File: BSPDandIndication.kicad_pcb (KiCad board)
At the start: 2 copper layers, 51 parts, among them J1 SafetyIN, J2 Masa, J3 12VTelem, J4 Sensors, J5 LED, J6 BSPD12OUT, J7 SafetyReturn, K1 FINDER-36.11, Q1 BC817, U1 LM1117-5.0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

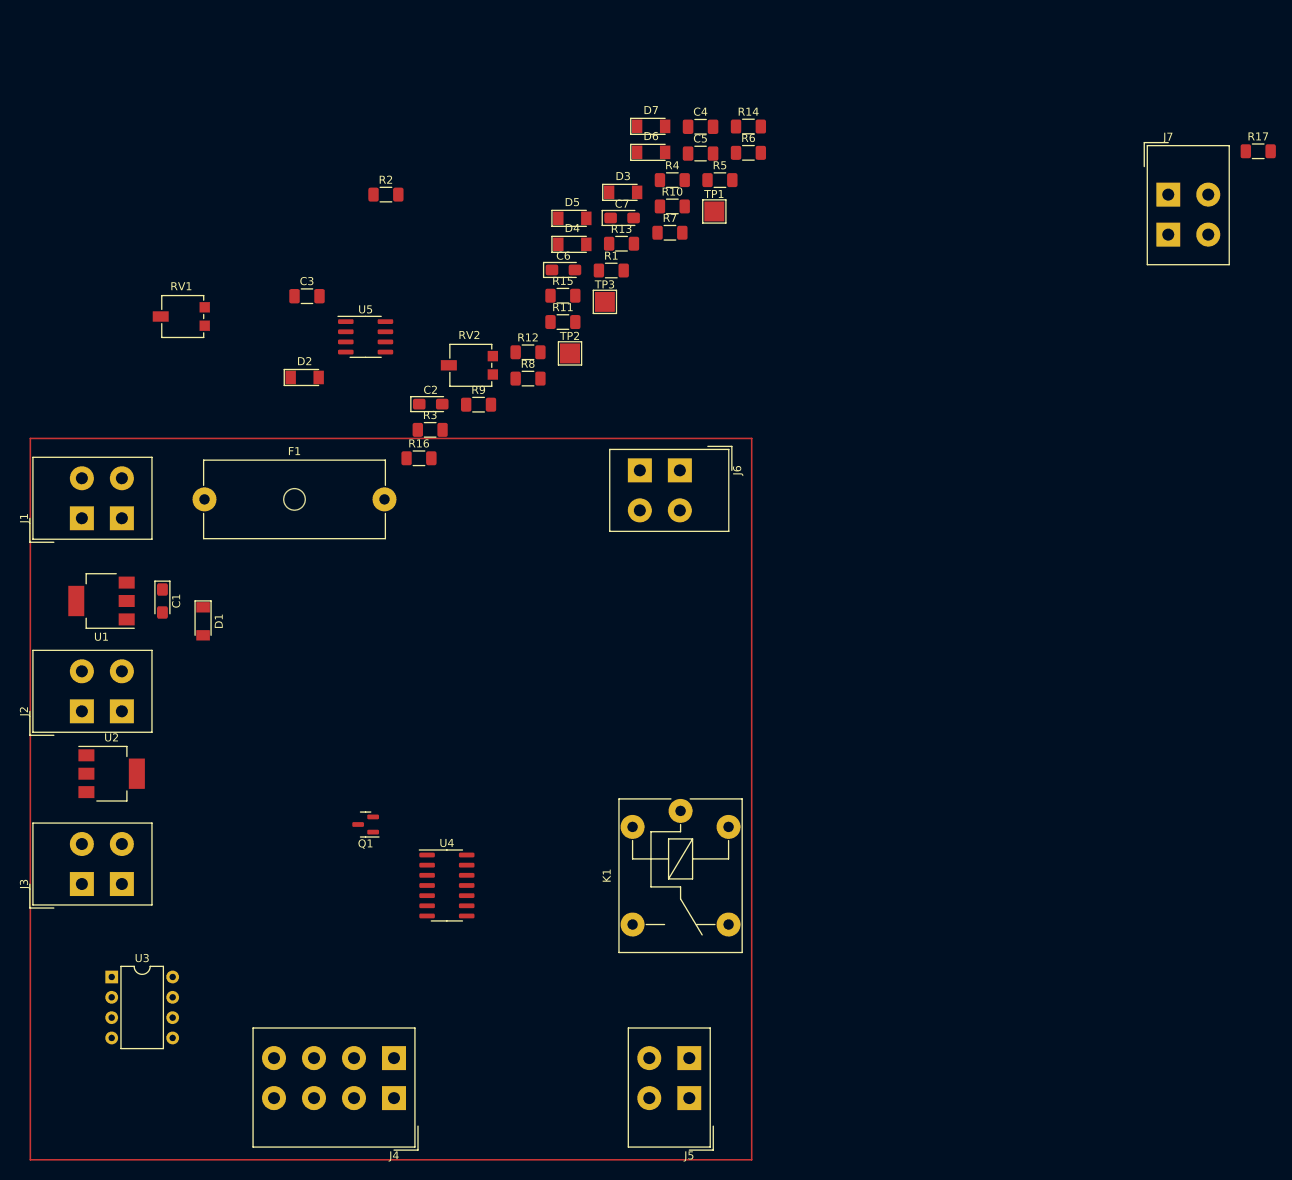
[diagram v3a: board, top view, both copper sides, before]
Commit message: Arrange components regarding PIC12f
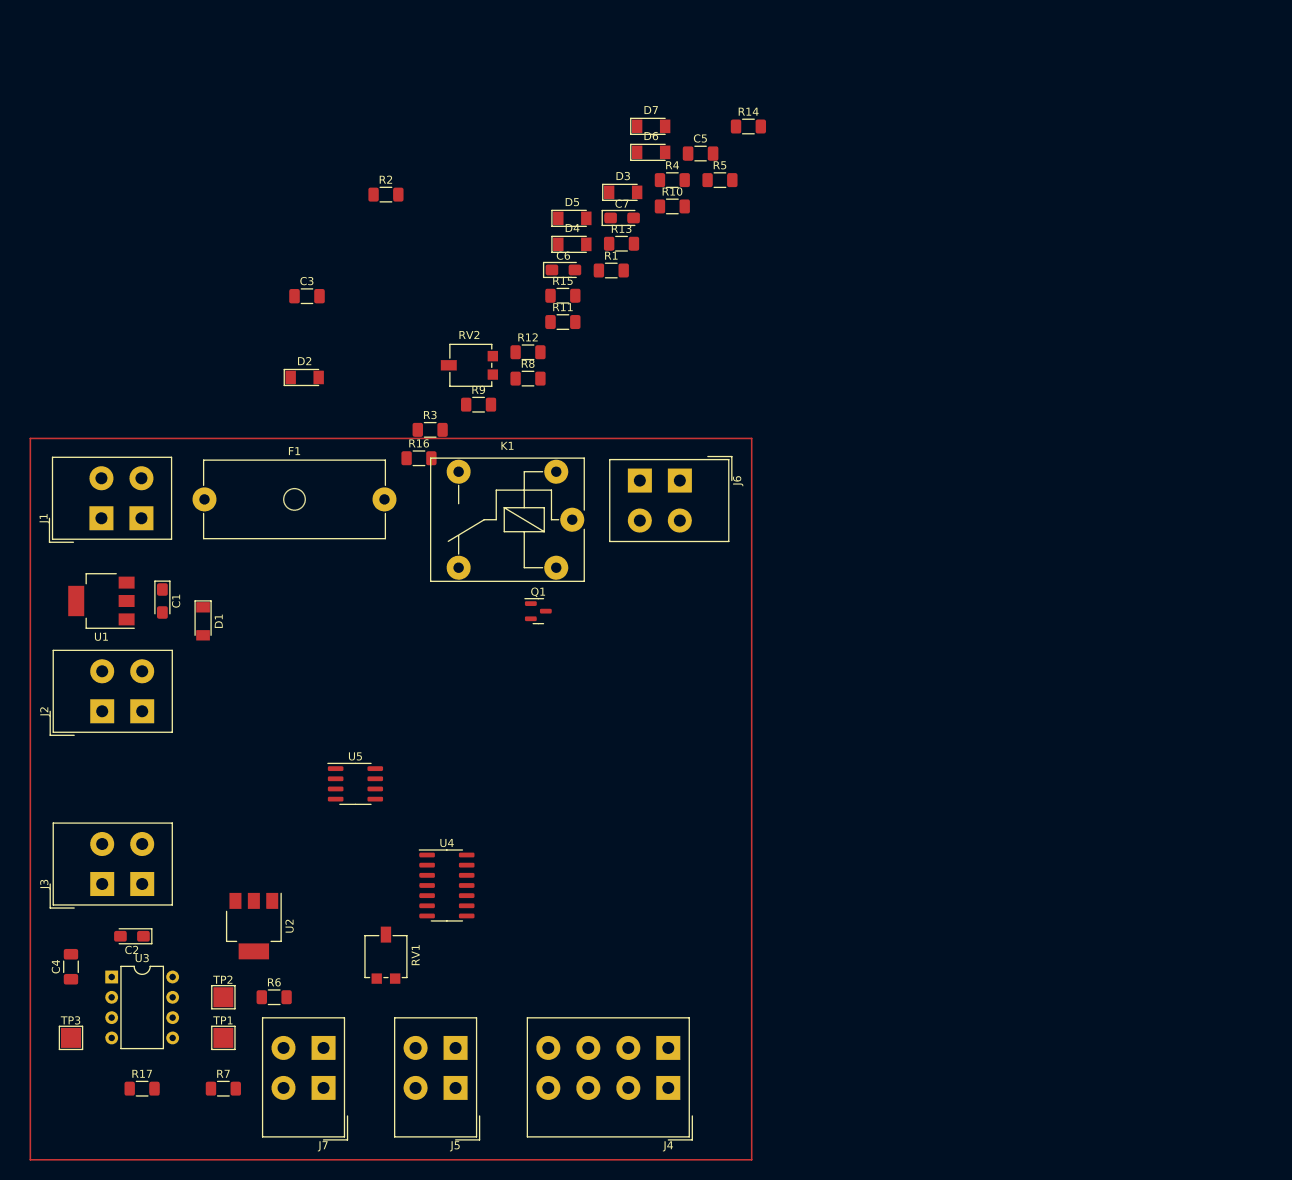
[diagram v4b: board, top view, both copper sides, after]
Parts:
- moved R17 182.2 mm to (30.5, 147.3)
- moved J7 153.7 mm to (53.2, 147.2), turned to 180 degrees
- moved C4 131.2 mm to (21.6, 132.1), turned to 90 degrees
- moved R6 121.1 mm to (47.0, 135.9)
- moved R7 120.7 mm to (40.6, 147.3)
- moved TP1 120.2 mm to (40.6, 141.0)
- moved TP3 113.7 mm to (21.6, 141.0)
- moved TP2 91.4 mm to (40.6, 135.9)
- moved RV1 83.9 mm to (61.0, 130.8), turned to -90 degrees
- moved C2 76.3 mm to (29.2, 128.3), turned to 180 degrees
- moved U5 55.9 mm to (57.1, 109.2)
- moved K1 38.8 mm to (84.2, 76.2), turned to 180 degrees
- moved Q1 34.3 mm to (80.0, 87.6), turned to 0 degrees
- moved J4 34.3 mm to (96.3, 147.2)
- moved J5 29.2 mm to (69.7, 147.2)
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
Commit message: First version of route
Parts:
- moved R2 102.3 mm to (86.4, 134.6), turned to -90 degrees
- moved R14 98.8 mm to (71.1, 119.4), turned to -90 degrees
- moved D3 90.5 mm to (91.4, 125.7), turned to 90 degrees
- moved R1 89.9 mm to (81.3, 134.6), turned to -90 degrees
- moved D7 89.3 mm to (51.8, 105.7), turned to -90 degrees
- moved D5 88.2 mm to (71.1, 125.7), turned to 90 degrees
- moved R10 84.6 mm to (77.5, 119.4), turned to 90 degrees
- moved C3 81.6 mm to (95.2, 116.8), turned to 90 degrees
- moved D6 79.2 mm to (87.6, 109.2), turned to 180 degrees
- moved C5 76.9 mm to (71.1, 101.6), turned to 90 degrees
- moved R3 74.0 mm to (91.4, 134.6), turned to -90 degrees
- moved D2 73.9 mm to (81.3, 125.7), turned to 90 degrees
- moved R12 72.4 mm to (62.2, 125.7), turned to 90 degrees
- moved C7 71.2 mm to (51.8, 98.2), turned to 90 degrees
- moved R15 66.9 mm to (46.7, 104.4), turned to 90 degrees
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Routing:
- net +5V: track 0.00 -> 150.8 mm, vias 0 -> 10
- net GND: track 0.00 -> 79.9 mm, vias 0 -> 15
- net /(A+B)C: track 0.00 -> 66.0 mm
- net +12V: track 0.00 -> 61.4 mm
- net Brake_ref: track 0.00 -> 60.7 mm
- net +12C: track 0.00 -> 58.6 mm
- net TPS: track 0.00 -> 38.3 mm, vias 0 -> 2
- net Net-(D2-Pad1): track 0.00 -> 37.6 mm, vias 0 -> 4
- net 12V_Telem: track 0.00 -> 37.0 mm
- net Net-(K1-Pad11): track 0.00 -> 31.0 mm
- net Brake1: track 0.00 -> 29.7 mm
- net Brake2: track 0.00 -> 29.6 mm
- net Net-(C4-Pad1): track 0.00 -> 28.7 mm
- net RELAY: track 0.00 -> 27.9 mm
- net Net-(R6-Pad2): track 0.00 -> 27.0 mm
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- added copper zone on B.Cu, net GND

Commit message: Fix DRC issues
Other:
- board outline added: 90.2 x 90.2 mm
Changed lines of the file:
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@@
     (property "Sheetname" "")
     (attr through_hole)
-    (fp_text reference "J4" (at 0 -7.2) (layer "F.SilkS")
+    (fp_text reference "J4" (at 0.5295 -7.2045) (layer "F.SilkS")
       (effects (font (size 1 1) (thickness 0.15)))
     )
@@
     )
   )
-  (gr_rect (start 16.51 156.21) (end 106.68 66.04) (layer "F.Cu") (width 0.2) (fill none))
+  (gr_rect (start 16.51 156.21) (end 106.68 66.04) (layer "Edge.Cuts") (width 0.2) (fill none))
   (segment (start 57.7725 76.6675) (end 60.78 73.66) (width 1) (layer "F.Cu") (net 1))
   (segment (start 57.7725 81.6455) (end 56.628 82.79) (width 1) (layer "F.Cu") (net 1))

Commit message: Add logo to PCB and final edit
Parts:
- added Log1: LOGO, Logo:r6 logo, F.Cu at (28.7, 50.3)
- moved TP2 53.6 mm to (40.4, 82.3)
- moved C4 52.7 mm to (23.2, 79.4)
- moved U3 52.7 mm to (28.3, 80.7)
- moved C6 52.7 mm to (53.7, 32.4)
- moved D1 52.7 mm to (60.9, 32.4)
- moved R15 52.7 mm to (48.4, 51.7)
- moved R16 52.7 mm to (48.4, 46.3)
- moved R4 52.7 mm to (88.0, 41.3)
- moved R5 52.7 mm to (91.8, 41.3)
- moved R8 52.7 mm to (88.0, 50.2)
- moved R9 52.7 mm to (91.8, 50.2)
- moved RV1 52.7 mm to (99.4, 41.3)
- moved RV2 52.7 mm to (99.4, 50.2)
- moved U1 52.7 mm to (43.6, 32.4)
- moved C1 52.7 mm to (60.9, 28.6)
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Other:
- board text added: "GND"
- board text added: "TPS"
